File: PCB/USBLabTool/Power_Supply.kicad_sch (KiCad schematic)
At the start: 53 parts, among them J19 T_N5V, U10 Opamp_Quad, U11 DG403, U13 r1283, U14 ST1L05APU33R, U15 ST1L05APU33R, U16 LTC1983ES6-5#TRPBF, U9 Opamp_Quad

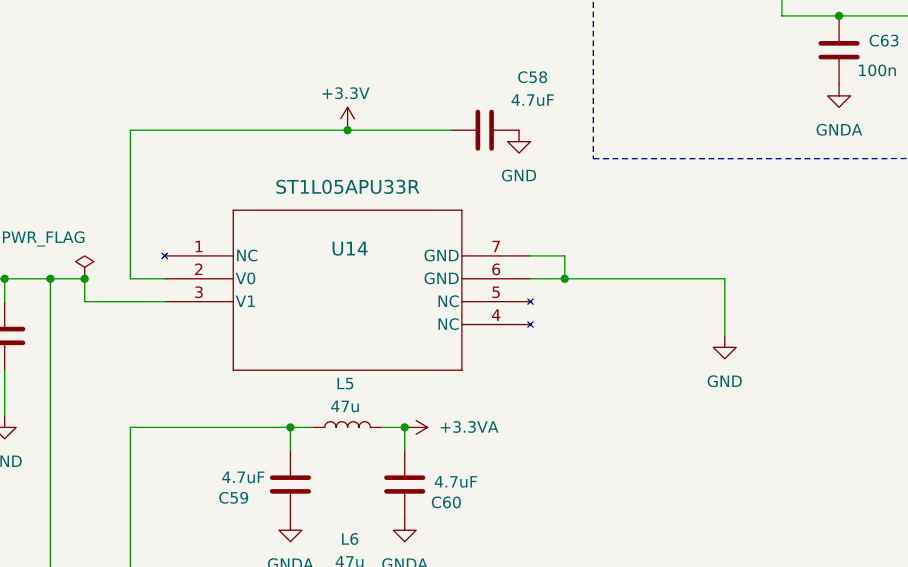
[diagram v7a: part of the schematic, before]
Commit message: Updated schematic and PCB
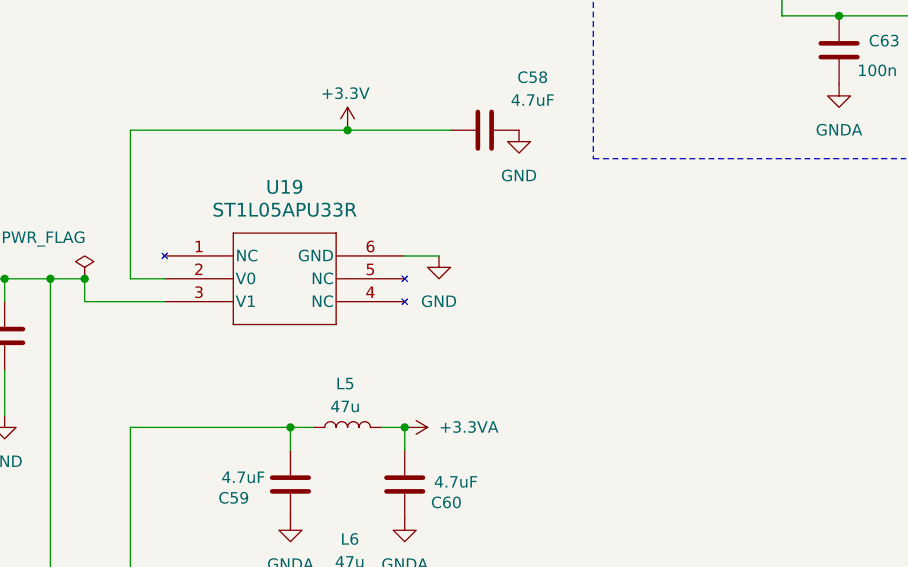
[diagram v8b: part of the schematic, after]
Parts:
- removed U14: ST1L05APU33R, DFN_5APU33R_STM, symbol ST1L05APU33R:ST1L05APU33R
- added U19: ST1L05APU33R, DFN_5APU33R_STM, symbol USBLabTool:ST1L05APU33R
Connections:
- net +3.3V: now also U19.2 (V0)
- net GND: now also U19.6 (GND)
- net at C55.1, C56.1, D8.1 (K)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: now also U19.3 (V1)
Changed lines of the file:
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@@
 	)
 	(junction
-		(at 190.5 96.52)
-		(diameter 0)
-		(color 0 0 0 0)
-	)
-	(junction
 		(at 62.23 100.33)
 		(diameter 0)
@@
 	(wire
 		(pts
-			(xy 190.5 93.98) (xy 190.5 96.52)
-		)
-		(stroke
-			(width 0)
-			(type default)
-		)
-	)
-	(wire
-		(pts
 			(xy 62.23 115.57) (xy 62.23 110.49)
 		)
@@
 	(wire
 		(pts
-			(xy 186.69 96.52) (xy 190.5 96.52)
-		)
-		(stroke
-			(width 0)
-			(type default)
-		)
-	)
-	(wire
-		(pts
 			(xy 213.36 48.1076) (xy 213.36 45.72)
 		)
@@
 	(wire
 		(pts
-			(xy 49.53 80.01) (xy 49.53 82.55)
+			(xy 172.72 93.98) (xy 176.53 93.98)
 		)
 		(stroke
@@
 	(wire
 		(pts
-			(xy 186.69 93.98) (xy 190.5 93.98)
+			(xy 49.53 80.01) (xy 49.53 82.55)
 		)
 		(stroke
@@
 	(wire
 		(pts
-			(xy 190.5 96.52) (xy 208.28 96.52)
-		)
-		(stroke
-			(width 0)
-			(type default)
-		)
-	)
-	(wire
-		(pts
 			(xy 137.16 99.06) (xy 137.16 96.52)
 		)
@@
 	(wire
 		(pts
-			(xy 208.28 96.52) (xy 208.28 102.87)
-		)
-		(stroke
-			(width 0)
-			(type default)
-		)
-	)
-	(wire
-		(pts
 			(xy 124.46 39.37) (xy 124.46 44.45)
 		)
@@
 	)
 	(symbol
+		(lib_name "GND_10")
+		(lib_id "power:GND")
+		(at 176.53 93.98 0)
+		(unit 1)
+		(exclude_from_sim no)
+		(in_bom yes)
+		(on_board yes)
+		(dnp no)
+		(fields_autoplaced yes)
+		(property "Reference" "#PWR0112"
+			(at 176.53 100.33 0)
+			(effects
+				(font
+					(size 1.27 1.27)
+				)
+				(hide yes)
+			)
+		)
+		(property "Value" "GND"
+			(at 176.53 99.06 0)
+			(effects
+				(font
+					(size 1.27 1.27)
+				)
+			)
+		)
+		(property "Footprint" ""
+			(at 176.53 93.98 0)
+			(effects
+				(font
+					(size 1.27 1.27)
+				)
+				(hide yes)
+			)
+		)
+		(property "Datasheet" ""
+			(at 176.53 93.98 0)
+			(effects
+				(font
+					(size 1.27 1.27)
+				)
+				(hide yes)
+			)
+		)
+		(property "Description" ""
+			(at 176.53 93.98 0)
+			(effects
+				(font
+					(size 1.27 1.27)
+				)
+				(hide yes)
+			)
+		)
+		(pin "1"
+		)
+		(instances
+			(project "USBLabTool"
+				(path "/b5440f7d-90d5-417e-adc2-aa6b11e5424d/eb849fef-899c-46da-8ce0-ed0caaa370cf"
+					(reference "#PWR0112")
+					(unit 1)
+				)
+			)
+		)
+	)
+	(symbol
 		(lib_id "Device:L")
 		(at 166.37 130.81 90)
@@
 	)
 	(symbol
+		(lib_id "USBLabTool:ST1L05APU33R")
+		(at 146.05 96.52 0)
+		(unit 1)
+		(exclude_from_sim no)
+		(in_bom yes)
+		(on_board yes)
+		(dnp no)
+		(fields_autoplaced yes)
+		(property "Reference" "U19"
+			(at 159.385 86.36 0)
+			(effects
+				(font
+					(size 1.524 1.524)
+				)
+			)
+		)
+		(property "Value" "ST1L05APU33R"
+			(at 159.385 88.9 0)
+			(effects
+				(font
+					(size 1.524 1.524)
+				)
+			)
+		)
+		(property "Footprint" "DFN_5APU33R_STM"
+			(at 146.05 96.52 0)
+			(effects
+				(font
+					(size 1.27 1.27)
+					(italic yes)
+				)
+				(hide yes)
+			)
+		)
+		(property "Datasheet" "ST1L05APU33R"
+			(at 146.05 96.52 0)
+			(effects
+				(font
+					(size 1.27 1.27)
+					(italic yes)
+				)
+				(hide yes)
+			)
+		)
+		(property "Description" ""
+			(at 146.05 93.98 0)
+			(effects
+				(font
+					(size 1.27 1.27)
+				)
+				(hide yes)
+			)
+		)
+		(pin "4"
+		)
+		(pin "6"
+		)
+		(pin "1"
+		)
+		(pin "2"
+		)
+		(pin "5"
+		)
+		(pin "3"
+		)
+		(instances
+			(project ""
+				(path "/b5440f7d-90d5-417e-adc2-aa6b11e5424d/eb849fef-899c-46da-8ce0-ed0caaa370cf"
+					(reference "U19")
+					(unit 1)
+				)
+			)
+		)
+	)
+	(symbol
 		(lib_name "GND_13")
 		(lib_id "power:GND")
@@
 	)
 	(symbol
-		(lib_name "GND_10")
-		(lib_id "power:GND")
-		(at 208.28 102.87 0)
-		(unit 1)
-		(exclude_from_sim no)
-		(in_bom yes)
-		(on_board yes)
-		(dnp no)
-		(fields_autoplaced yes)
-		(property "Reference" "#PWR0112"
-			(at 208.28 109.22 0)
-			(effects
-				(font
-					(size 1.27 1.27)
-				)
-				(hide yes)
-			)
-		)
-		(property "Value" "GND"
-			(at 208.28 107.95 0)
-			(effects
-				(font
-					(size 1.27 1.27)
-				)
-			)
-		)
-		(property "Footprint" ""
-			(at 208.28 102.87 0)
-			(effects
-				(font
-					(size 1.27 1.27)
-				)
-				(hide yes)
-			)
-		)
-		(property "Datasheet" ""
-			(at 208.28 102.87 0)
-			(effects
-				(font
-					(size 1.27 1.27)
-				)
-				(hide yes)
-			)
-		)
-		(property "Description" ""
-			(at 208.28 102.87 0)
-			(effects
-				(font
-					(size 1.27 1.27)
-				)
-				(hide yes)
-			)
-		)
-		(pin "1"
-		)
-		(instances
-			(project "USBLabTool"
-				(path "/b5440f7d-90d5-417e-adc2-aa6b11e5424d/eb849fef-899c-46da-8ce0-ed0caaa370cf"
-					(reference "#PWR0112")
-					(unit 1)
-				)
-			)
-		)
-	)
-	(symbol
 		(lib_id "Device:C")
 		(at 231.14 71.12 0)
@@
 					(unit 1)
 				)
-			)
-		)
-	)
-	(symbol
-		(lib_id "ST1L05APU33R:ST1L05APU33R")
-		(at 146.05 93.98 0)
-		(unit 1)
-		(exclude_from_sim no)
-		(in_bom yes)
-		(on_board yes)
-		(dnp no)
-		(property "Reference" "U14"
-			(at 166.624 93.218 0)
-			(effects
-				(font
-					(size 1.524 1.524)
-				)
-			)
-		)
-		(property "Value" "ST1L05APU33R"
-			(at 166.37 86.36 0)
-			(effects
-				(font
-					(size 1.524 1.524)
-				)
-			)
-		)
-		(property "Footprint" "DFN_5APU33R_STM"
-			(at 146.05 93.98 0)
-			(effects
-				(font
-					(size 1.27 1.27)
-					(italic yes)
-				)
-				(hide yes)
-			)
-		)
-		(property "Datasheet" "ST1L05APU33R"
-			(at 146.05 93.98 0)
-			(effects
-				(font
-					(size 1.27 1.27)
-					(italic yes)
-				)
-				(hide yes)
-			)
-		)
-		(property "Description" ""
-			(at 146.05 93.98 0)
-			(effects
-				(font
-					(size 1.27 1.27)
-				)
-				(hide yes)
-			)
-		)
-		(pin "3"
-		)
-		(pin "6"
-		)
-		(pin "1"
-		)
-		(pin "7"
-		)
-		(pin "4"
-		)
-		(pin "5"
-		)
-		(pin "2"
-		)
-		(instances
-			(project ""
-				(path "/b5440f7d-90d5-417e-adc2-aa6b11e5424d/eb849fef-899c-46da-8ce0-ed0caaa370cf"
-					(reference "U14")
-					(unit 1)
-				)
